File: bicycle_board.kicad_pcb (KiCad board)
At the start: 2 copper layers, 40.9 x 84.4 mm, 151 parts, among them J1 Micro_SD_Card, J10 USB_A, J11 Conn_01x04, J12 Conn_01x01, J13 Conn_01x04, J14 Conn_01x01, J2 USB_C_Receptacle_USB2.0_16P, J3 Conn_01x02, J4 Conn_01x02, J5 Conn_01x08, J6 Conn_01x04, J7 Conn_01x05, J8 Conn_01x02, J9 Conn_01x06, Q1 Q_NMOS_GSD, Q4 Q_NMOS_GSD, Q6 Si2302, Q7 Si2302, Q8 Q_PMOS_GSD, Q9 Q_PMOS_GSD, U1 TP4056, U10 USBLC6-2SC6, U11 BMP280, U12 MMC5633NJL, U13 NS4168, U14 ESP32-C3-WROOM-02U, U15 CH32V203C8T6, U16 PS7516, U17 TXB0108PW, U18 USBLC6-2SC6, U2 SGM2039, U3 IIM-42652, U4 QMI8610, U5 AHT20, U6 SGM2033-1.8, U7 74HC595, U8 SGM8040-1, U9 PCA9306DC1, Y1 12MHz, Y2 32.768kHz

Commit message: 工程中修改为正确芯片型号QMC6308,ICM-42688-P，按数据手册更新供电滤波电容值
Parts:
- C15: value 100nF -> 2.2uF
- R32: value R -> 330
- U12: value MMC5633NJL -> QMC6308
- U3: value IIM-42652 -> ICM-42688-P
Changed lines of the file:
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@@
 			)
 		)
-		(property "Value" "MMC5633NJL"
+		(property "Value" "QMC6308"
 			(at 0 2.25 0)
 			(layer "F.Fab")
@@
 			)
 		)
-		(property "Datasheet" "http://www.memsic.com/uploadfiles/2020/08/20200827165106864.pdf"
+		(property "Datasheet" "https://www.qstcorp.com/upload/pdf/202202/13-52-15%20QMC6308%20Datasheet%20Rev.%20F(1).pdf"
 			(at 0 0 0)
 			(unlocked yes)
@@
 			)
 		)
-		(property "Description" "3-axis AMR Magnetometer, 30 G, I2C & I3C  Interface, 2mG RMS, WLP-4"
+		(property "Description" "3-axis AMR Magnetometer, 30 G, I2C Interface, 2mG RMS, WLP-4"
 			(at 0 0 0)
 			(unlocked yes)
@@
 			)
 		)
-		(property "Value" "100nF"
+		(property "Value" "2.2uF"
 			(at 0 1.16 90)
 			(layer "F.Fab")
@@
 			)
 		)
-		(property "Value" "IIM-42652"
+		(property "Value" "ICM-42688-P"
 			(at 0 2.5 0)
 			(layer "F.Fab")
@@
 			)
 		)
-		(property "Datasheet" "https://invensense.tdk.com/wp-content/uploads/2021/01/ds-000440_iim-42652-datasheet.pdf"
+		(property "Datasheet" "https://product.tdk.com.cn/system/files/dam/doc/product/sensor/mortion-inertial/imu/data_sheet/ds-000347-icm-42688-p-v1.6.pdf"
 			(at 0 0 0)
 			(unlocked yes)
@@
 			)
 		)
-		(property "Value" "R"
+		(property "Value" "330"
 			(at 0 1.43 90)
 			(layer "F.Fab")

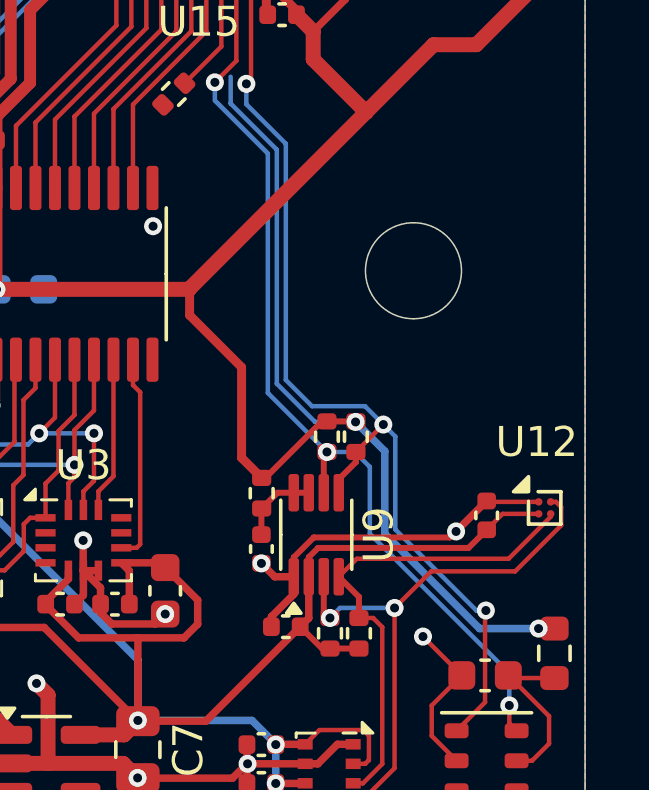
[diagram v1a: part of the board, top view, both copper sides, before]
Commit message: 添加第二个磁力计QMC7983
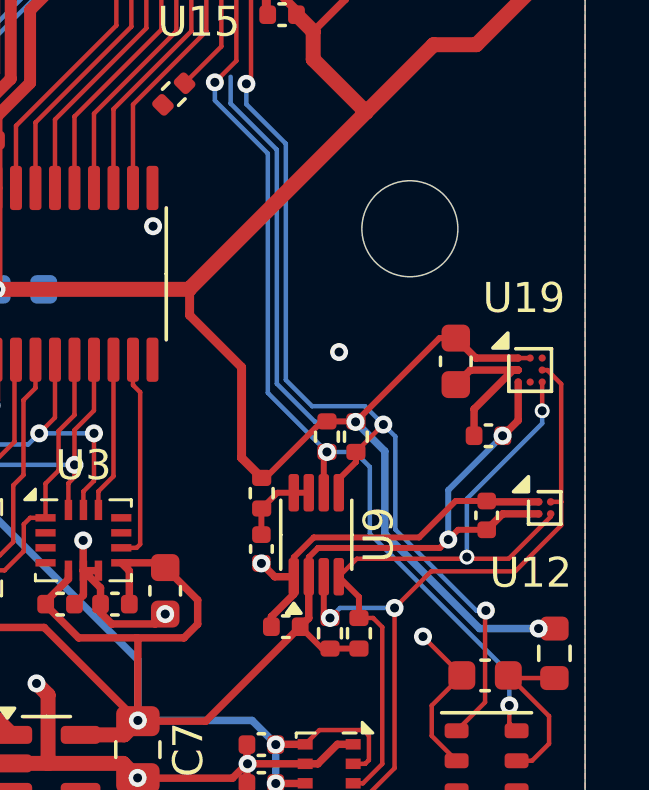
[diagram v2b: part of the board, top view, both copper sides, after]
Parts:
- added C59: 4.7uF, Capacitor_SMD:C_0603_1608Metric, F.Cu at (137.2, 124.4)
- added C60: 100nF, Capacitor_SMD:C_0402_1005Metric, F.Cu at (138.3, 126.9)
- added U19: QMC7983, Library:WLP-8_1.2x1.2mm_Layout3x3_P0.4mm_Pad0.24mm, F.Cu at (139.7, 124.7)
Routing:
- net +3.3V: track 374.2 -> 381.4 mm
- net /sensors/SDA1V8: track 16.3 -> 23.2 mm, vias 0 -> 2
- net +1V8: track 72.1 -> 78.3 mm, vias 5 -> 7
- net GND: track 262.3 -> 267.4 mm
- net /sensors/SCL1V8: track 18.7 -> 23.5 mm
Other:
- outline, holes or cut-outs redrawn

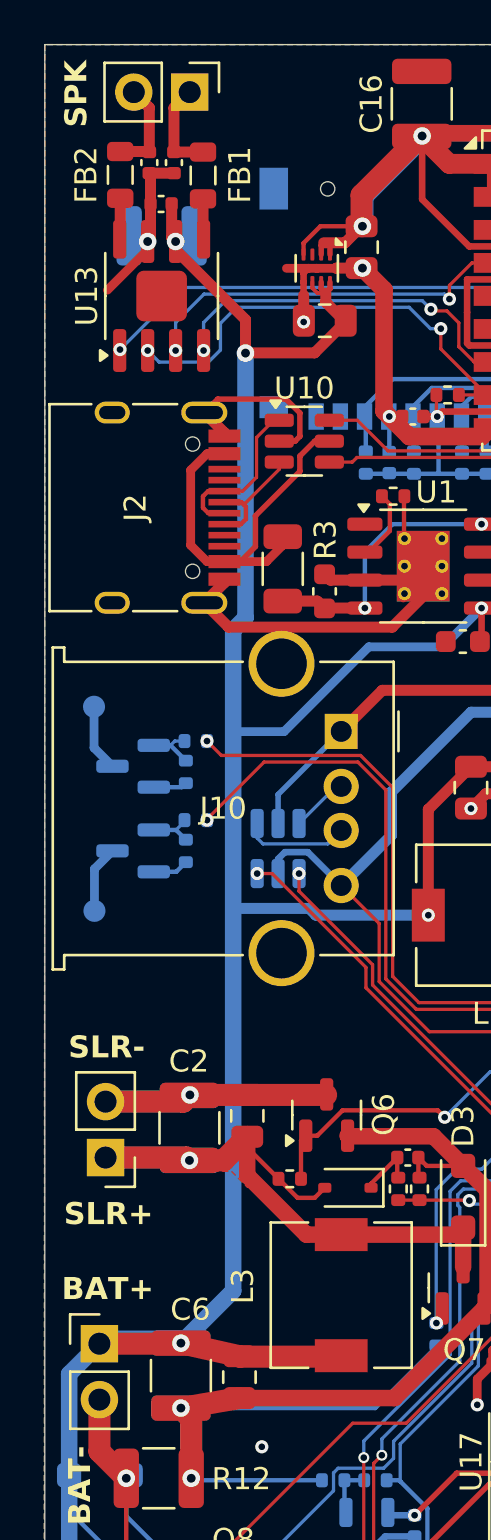
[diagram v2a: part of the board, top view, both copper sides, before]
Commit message: 按数据手册调整NS4168布线，电源GND改用单点连接，加粗电源和喇叭走线到0.6mm，中心焊盘连接GND增强散热性能
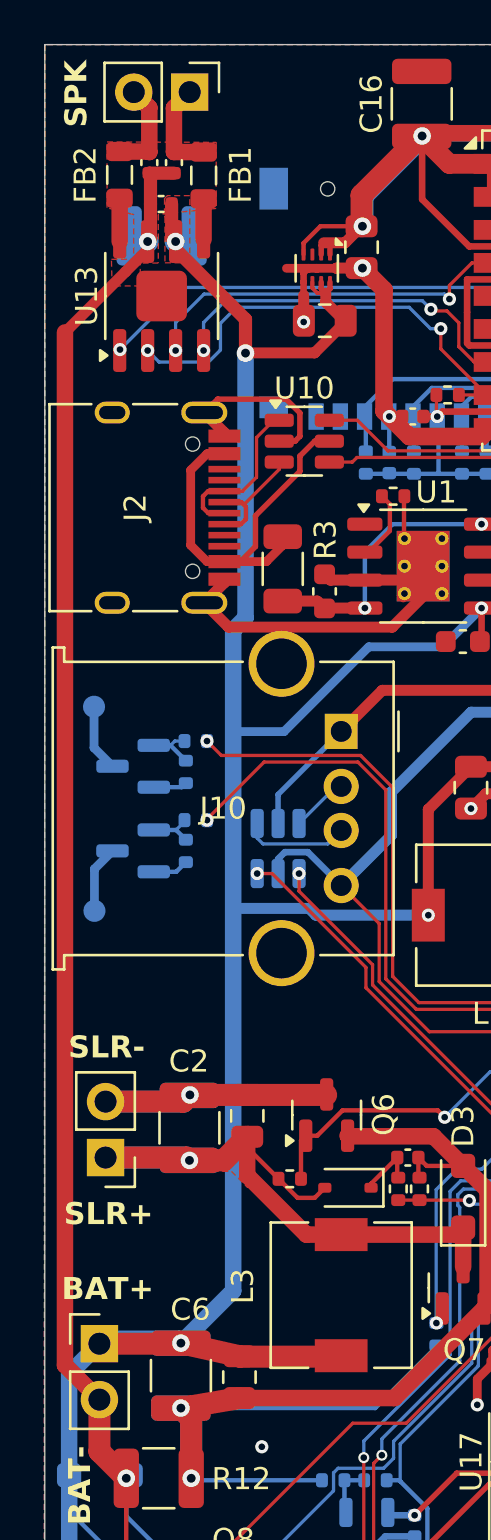
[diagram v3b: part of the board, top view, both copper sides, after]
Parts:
- added NT1: NetTie_2, NetTie:NetTie-2_SMD_Pad0.5mm, F.Cu at (104.6, 67.1)
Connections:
- C36 pad 2: GND -> /GND_audio
- C37 pad 2: GND -> /GND_audio
- C38 pad 2: GND -> /GND_audio
- C39 pad 2: GND -> /GND_audio
- U13 pad 7: GND -> /GND_audio
- U13 pad 9: (no net) -> GND
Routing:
- net GND: track 267.4 -> 312.2 mm, vias 34 -> 33
- net /GND_audio: track 0.00 -> 6.04 mm, vias 0 -> 1
- added copper zone on F.Cu, net /GND_audio

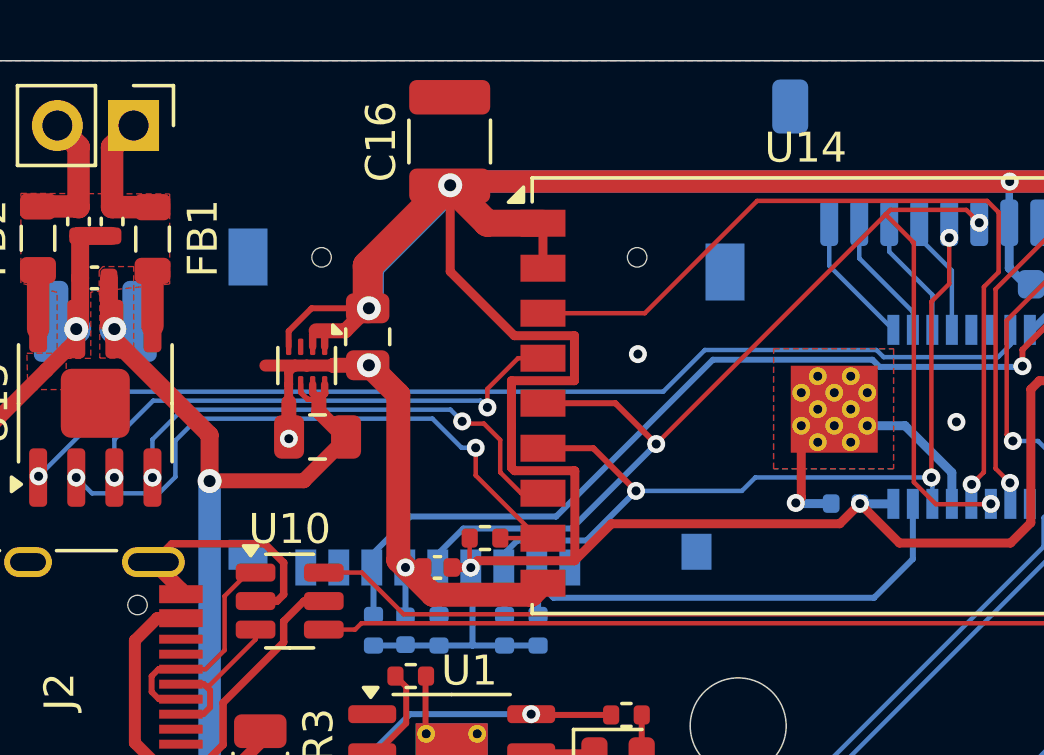
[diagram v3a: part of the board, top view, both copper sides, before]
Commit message: 调整电源走线，ESP32左侧添加3.3V覆铜
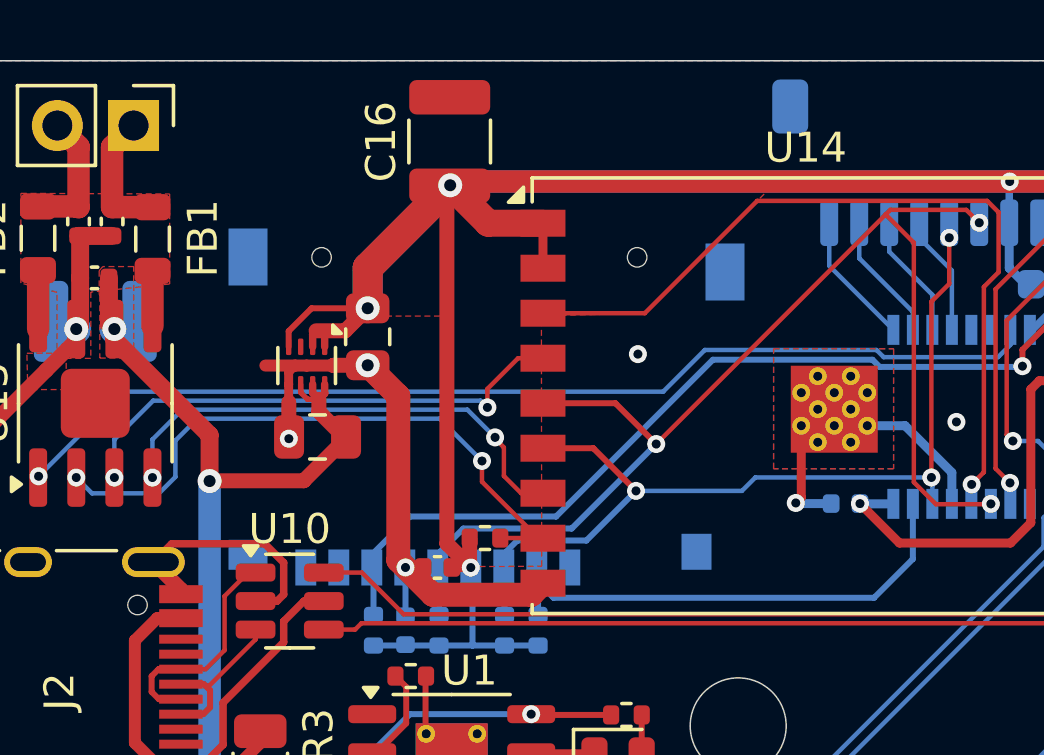
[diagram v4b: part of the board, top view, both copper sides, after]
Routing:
- net +3.3V: track 381.4 -> 361.0 mm

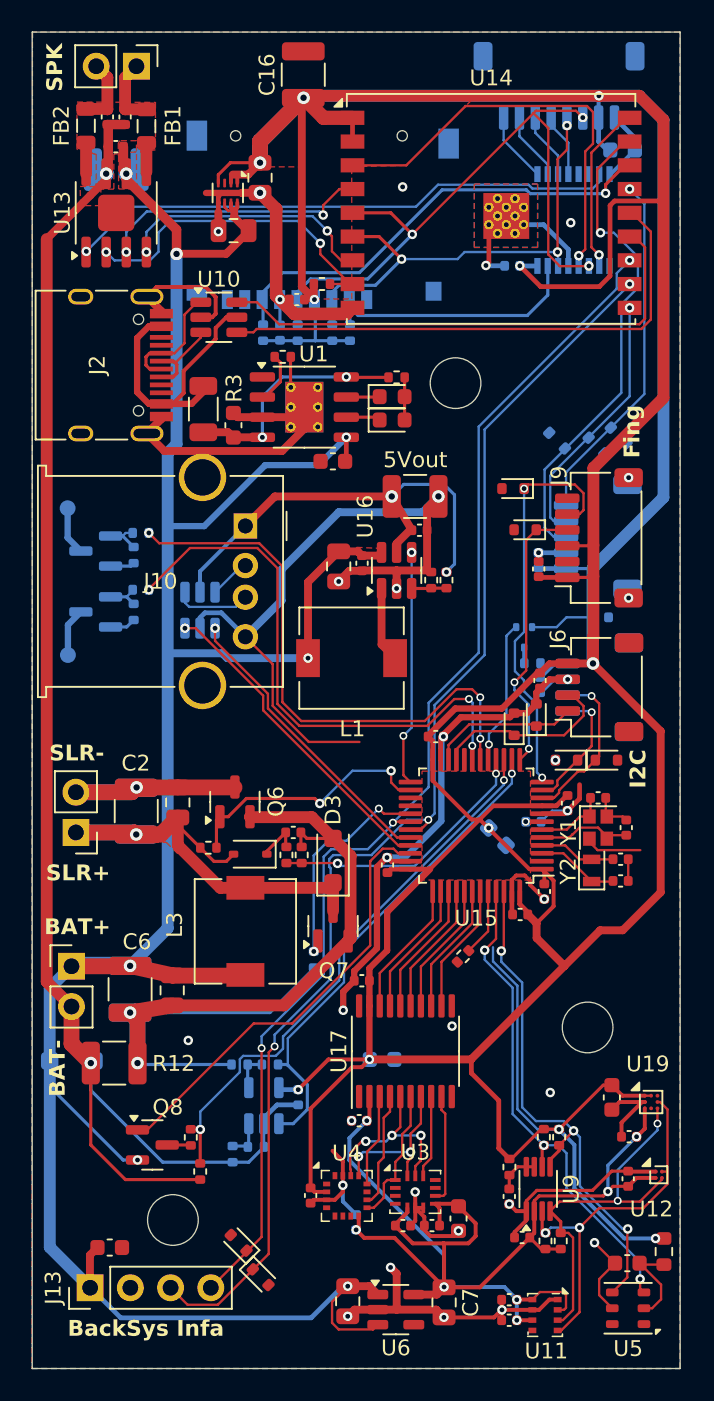
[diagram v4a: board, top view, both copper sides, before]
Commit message: GND布线，检查回路完整性
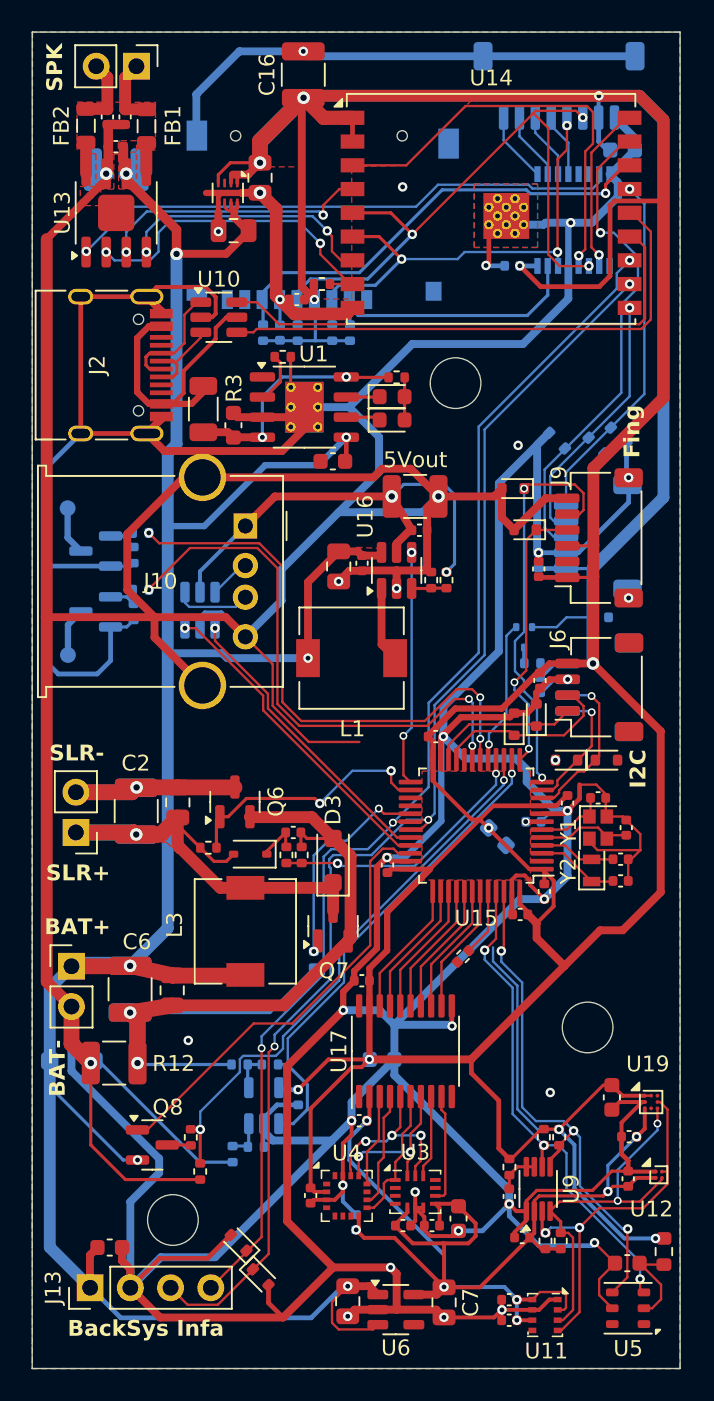
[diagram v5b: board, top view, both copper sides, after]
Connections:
- U1 pad 1: unconnected-(U1-TEMP-Pad1) -> GND
- U7 pad 6: /SPI_CS_STM32 -> unconnected-(U7-QG-Pad6)
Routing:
- net GND: track 312.2 -> 690.2 mm, vias 33 -> 35

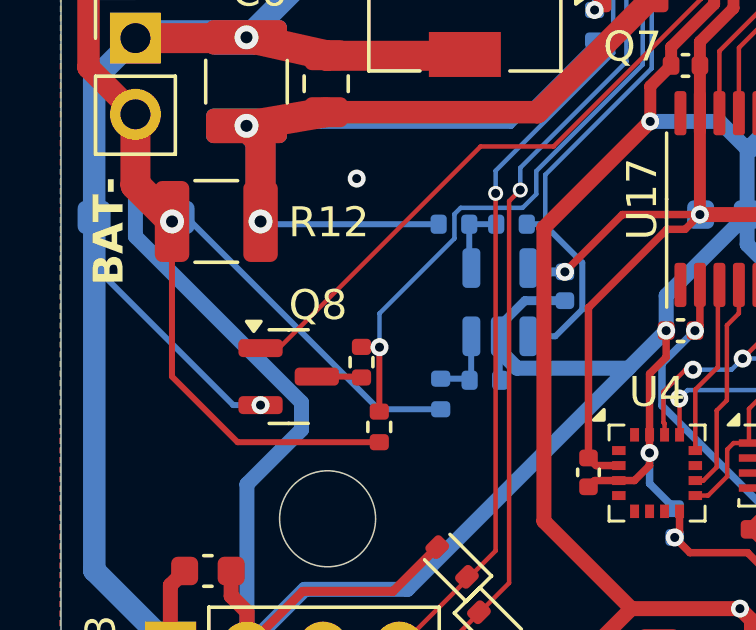
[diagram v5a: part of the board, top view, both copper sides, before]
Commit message: 太阳能充电电流测量GND回路用NetTie分割为不同的网络，避免被覆铜覆盖
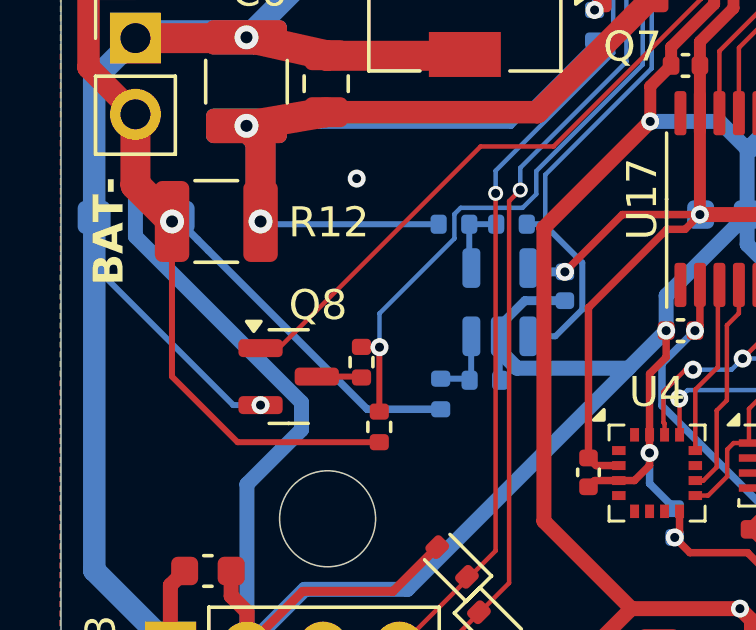
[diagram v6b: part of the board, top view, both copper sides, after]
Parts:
- added NT2: NetTie_2, NetTie:NetTie-2_SMD_Pad0.5mm, B.Cu at (105.3, 123.0)
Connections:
- R18 pad 1: GND -> Net-(NT2-Pad1)
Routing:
- net GND: track 690.2 -> 679.7 mm
- net Net-(NT2-Pad1): track 0.00 -> 9.94 mm
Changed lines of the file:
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@@
 	(net 136 "unconnected-(U19-NC-PadA3)")
 	(net 137 "/GND_audio")
+	(net 138 "Net-(NT2-Pad1)")
 	(footprint "Resistor_SMD:R_0402_1005Metric"
 		(layer "F.Cu")
@@
 		)
 	)
+	(footprint "NetTie:NetTie-2_SMD_Pad0.5mm"
+		(layer "B.Cu")
+		(at 105.316777 122.996777 135)
+		(descr "Net tie, 2 pin, 0.5mm square SMD pads")
+		(tags "net tie")
+		(property "Reference" "NT2"
+			(at 0 1.2 -45)
+			(layer "B.SilkS")
+			(hide yes)
+			(effects
+				(font
+					(size 1 1)
+					(thickness 0.15)
+				)
+				(justify mirror)
+			)
+		)
+		(property "Value" "NetTie_2"
+			(at 0 -1.2 -45)
+			(layer "B.Fab")
+			(hide yes)
+			(effects
+				(font
+					(size 1 1)
+					(thickness 0.15)
+				)
+				(justify mirror)
+			)
+		)
+		(property "Footprint" "NetTie:NetTie-2_SMD_Pad0.5mm"
+			(at 0 0 -45)
+			(unlocked yes)
+			(layer "B.Fab")
+			(hide yes)
+			(effects
+				(font
+					(size 1.27 1.27)
+					(thickness 0.15)
+				)
+				(justify mirror)
+			)
+		)
+		(property "Datasheet" ""
+			(at 0 0 -45)
+			(unlocked yes)
+			(layer "B.Fab")
+			(hide yes)
+			(effects
+				(font
+					(size 1.27 1.27)
+					(thickness 0.15)
+				)
+				(justify mirror)
+			)
+		)
+		(property "Description" "Net tie, 2 pins"
+			(at 0 0 -45)
+			(unlocked yes)
+			(layer "B.Fab")
+			(hide yes)
+			(effects
+				(font
+					(size 1.27 1.27)
+					(thickness 0.15)
+				)
+				(justify mirror)
+			)
+		)
+		(property ki_fp_filters "Net*Tie*")
+		(sheetname "power")
+		(sheetfile "power.kicad_sch")
+		(attr exclude_from_pos_files exclude_from_bom allow_missing_courtyard)
+		(net_tie_pad_groups "1, 2")
+		(fp_poly
+			(pts
+				(xy -0.249999 0.125) (xy 0.249999 0.125) (xy 0.249999 -0.125) (xy -0.249999 -0.125)
+			)
+			(stroke
+				(width 0)
+				(type solid)
+			)
+			(fill solid)
+			(layer "B.Cu")
+		)
+		(pad "1" smd circle
+			(at -0.25 0 135)
+			(size 0.25 0.25)
+			(layers "B.Cu")
+			(net 138 "Net-(NT2-Pad1)")
+			(pinfunction "1")
+			(pintype "passive")
+		)
+		(pad "2" smd circle
+			(at 0.25 0 135)
+			(size 0.25 0.25)
+			(layers "B.Cu")
+			(net 2 "GND")
+			(pinfunction "2")
+			(pintype "passive")
+		)
+	)
 	(footprint "Capacitor_SMD:C_0603_1608Metric"
 		(layer "B.Cu")
@@
 			(layers "B.Cu" "B.Paste" "B.Mask")
 			(roundrect_rratio 0.25)
-			(net 2 "GND")
+			(net 138 "Net-(NT2-Pad1)")
 			(pintype "passive")
 		)
@@
 	)
 	(segment
+		(start 104.51 122.21)
+		(end 104.53 122.21)
+		(width 0.25)
+		(layer "B.Cu")
+		(net 2)
+	)
+	(segment
 		(start 120.5988 80.785)
 		(end 122.4898 82.676)
@@
 	)
 	(segment
-		(start 111.1697 128.4697)
-		(end 113.2398 128.4697)
-		(width 0.2)
+		(start 104.285 122.21)
+		(end 104.51 122.21)
+		(width 0.3)
 		(layer "B.Cu")
 		(net 2)
@@
 	)
 	(segment
+		(start 104.53 122.21)
+		(end 105.14 122.82)
+		(width 0.25)
+		(layer "B.Cu")
+		(net 2)
+	)
+	(segment
 		(start 138.114975 83.074975)
 		(end 138.114975 85.104975)
@@
 	)
 	(segment
-		(start 104.91 122.21)
-		(end 111.1697 128.4697)
-		(width 0.2)
-		(layer "B.Cu")
-		(net 2)
-	)
-	(segment
 		(start 133.5 97.98)
 		(end 134.395 97.98)
@@
 	)
 	(segment
-		(start 104.285 122.21)
-		(end 104.91 122.21)
-		(width 0.2)
-		(layer "B.Cu")
-		(net 2)
-	)
-	(segment
 		(start 126.55 101.59)
 		(end 126.42 101.72)
@@
 		(net 137)
 	)
+	(segment
+		(start 110.7897 128.4697)
+		(end 113.2398 128.4697)
+		(width 0.25)
+		(layer "B.Cu")
+		(net 138)
+	)
+	(segment
+		(start 105.493554 123.173554)
+		(end 110.7897 128.4697)
+		(width 0.25)
+		(layer "B.Cu")
+		(net 138)
+	)
 	(zone
